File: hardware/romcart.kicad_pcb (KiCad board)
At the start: 4 copper layers, 57.5 x 51 mm, 29 parts, among them J1 GAME BOY 32 CONTACTS, M1 Core2350B2 (31692), Q1 2N7002, U1 SN74LVC245APWR, U2 SN74LVC245APWR, U3 SN74LVC245APWR, U4 SN74LVC8T245PWR, U5 SN74LVC1G10DBVR, U6 SN74LVC1G332DBVR

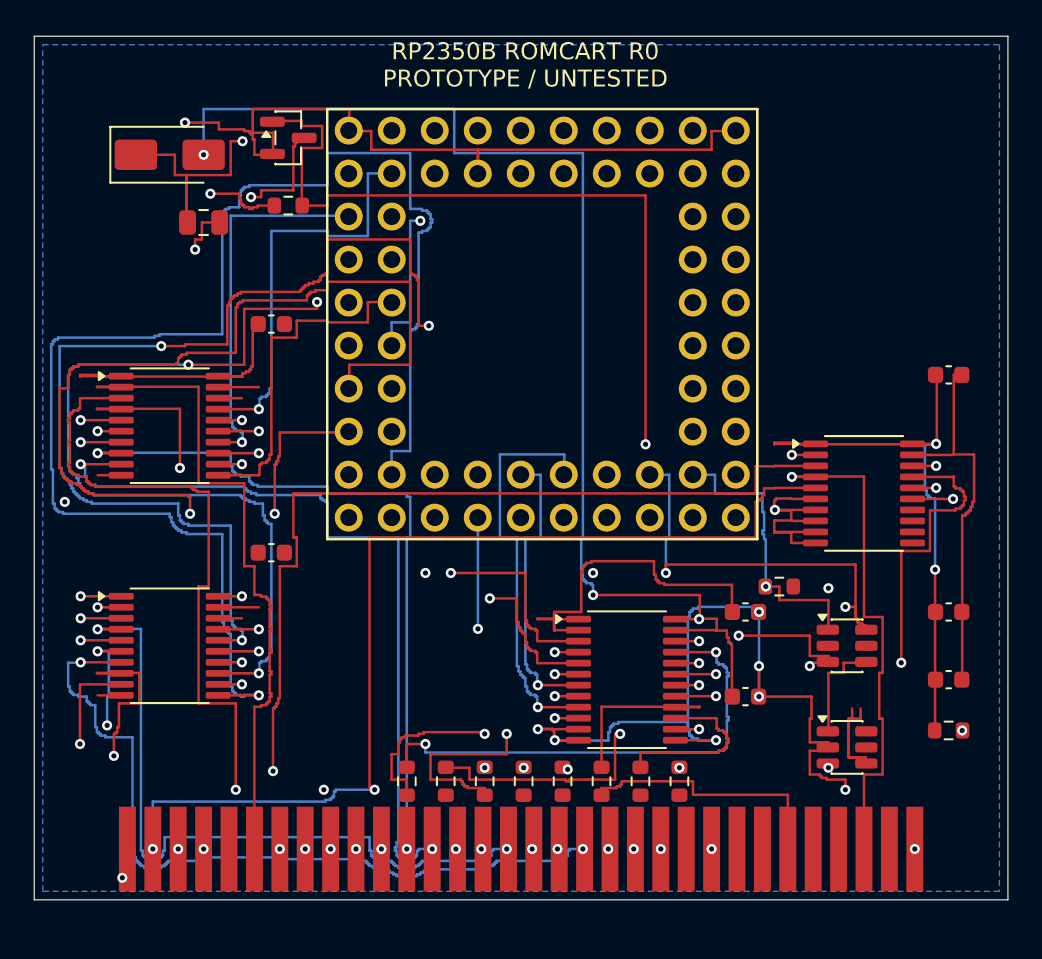
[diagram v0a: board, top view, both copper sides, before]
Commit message: Complete carrier routing and pass ERC DRC and schematic parity; refresh reviewed fabrication drafts
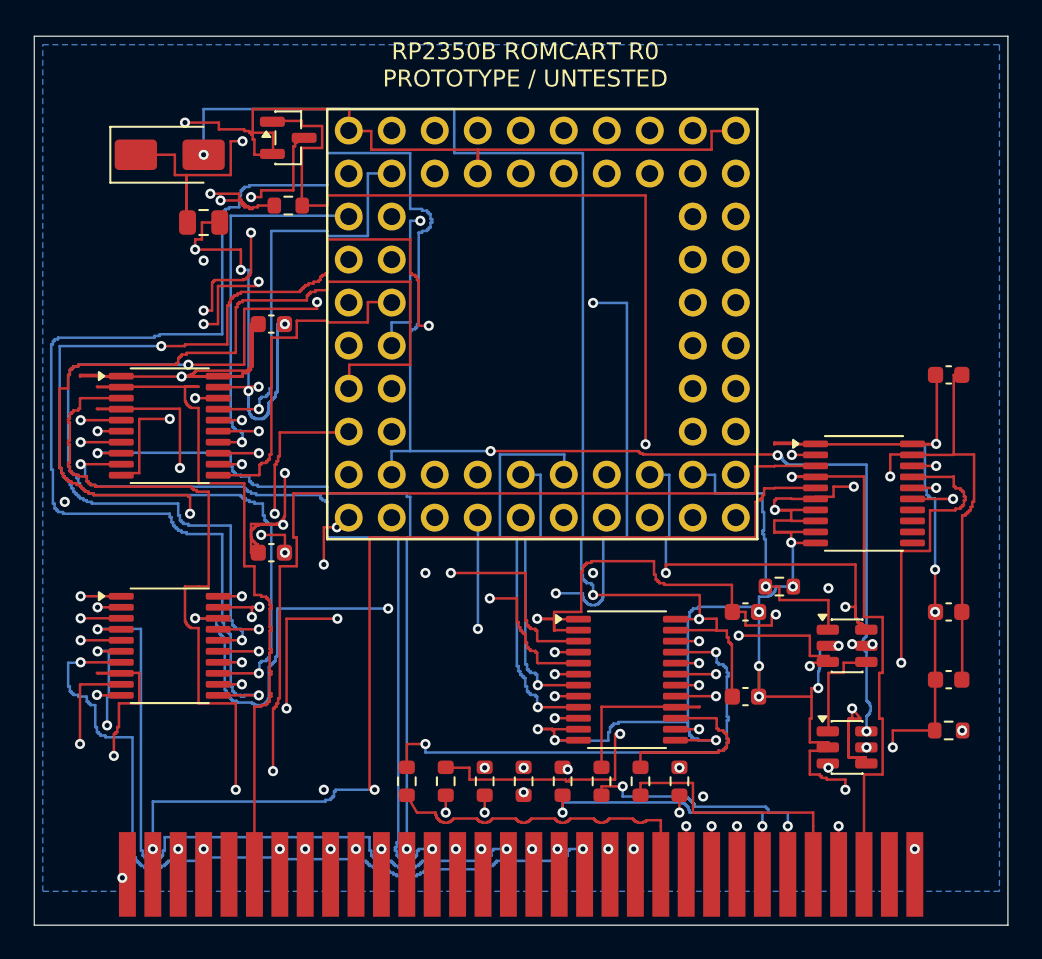
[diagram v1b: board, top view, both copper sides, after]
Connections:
- net +3V3 renamed /+3V3
- net +5V_GB renamed /+5V_GB
- net A0 renamed /A0
- net A0_3V3 renamed /A0_3V3
- net A1 renamed /A1
- net A10 renamed /A10
- net A10_3V3 renamed /A10_3V3
- net A11 renamed /A11
- net A11_3V3 renamed /A11_3V3
- net A12 renamed /A12
- net A12_3V3 renamed /A12_3V3
- net A13 renamed /A13
- net A13_3V3 renamed /A13_3V3
- net A14 renamed /A14
- net A14_3V3 renamed /A14_3V3
- net A15 renamed /A15
- net A15_3V3 renamed /A15_3V3
- net A1_3V3 renamed /A1_3V3
- net A2 renamed /A2
- net A2_3V3 renamed /A2_3V3
- net A3 renamed /A3
- net A3_3V3 renamed /A3_3V3
- net A4 renamed /A4
- net A4_3V3 renamed /A4_3V3
- net A5 renamed /A5
- net A5_3V3 renamed /A5_3V3
- net A6 renamed /A6
- net A6_3V3 renamed /A6_3V3
- net A7 renamed /A7
- net A7_3V3 renamed /A7_3V3
- net A8 renamed /A8
- net A8_3V3 renamed /A8_3V3
- net A9 renamed /A9
- net A9_3V3 renamed /A9_3V3
- net CLK renamed /CLK
- net CLK_3V3 renamed /CLK_3V3
- net D0 renamed /D0
- net D0_3V3 renamed /D0_3V3
- net D0_GB renamed /D0_GB
- net D1 renamed /D1
- net D1_3V3 renamed /D1_3V3
- net D1_GB renamed /D1_GB
- net D2 renamed /D2
- net D2_3V3 renamed /D2_3V3
- net D2_GB renamed /D2_GB
- net D3 renamed /D3
- net D3_3V3 renamed /D3_3V3
- net D3_GB renamed /D3_GB
- net D4 renamed /D4
- net D4_3V3 renamed /D4_3V3
- net D4_GB renamed /D4_GB
- net D5 renamed /D5
- net D5_3V3 renamed /D5_3V3
- net D5_GB renamed /D5_GB
- net D6 renamed /D6
- net D6_3V3 renamed /D6_3V3
- net D6_GB renamed /D6_GB
- net D7 renamed /D7
- net D7_3V3 renamed /D7_3V3
- net D7_GB renamed /D7_GB
- net GND renamed /GND
- net INHIBIT renamed /INHIBIT
- net MOD_VBUS renamed /MOD_VBUS
- net OE_L renamed /OE_L
- net RD_L renamed /RD_L
- net RD_L_3V3 renamed /RD_L_3V3
- net RESET_HOLD renamed /RESET_HOLD
- net RESET_L renamed /RESET_L
- net RESET_L_3V3 renamed /RESET_L_3V3
- net VALID renamed /VALID
- net WR_L renamed /WR_L
- net WR_L_3V3 renamed /WR_L_3V3
- J1 pad 31: (no net) -> unconnected-(J1-VIN-Pad31)
- J1 pad 5: (no net) -> unconnected-(J1-CS_L-Pad5)
- M1 pad 3V3_EN: (no net) -> unconnected-(M1-Pad3V3_EN)
- M1 pad ADC_VREF: (no net) -> unconnected-(M1-PadADC_VREF)
- M1 pad BOOTSEL: (no net) -> unconnected-(M1-PadBOOTSEL)
- M1 pad GP30: (no net) -> unconnected-(M1-PadGP30)
- M1 pad GP31: (no net) -> unconnected-(M1-PadGP31)
- M1 pad GP32: (no net) -> unconnected-(M1-PadGP32)
- M1 pad GP33: (no net) -> unconnected-(M1-PadGP33)
- M1 pad GP34: (no net) -> unconnected-(M1-PadGP34)
- M1 pad GP35: (no net) -> unconnected-(M1-PadGP35)
- M1 pad GP36: (no net) -> unconnected-(M1-PadGP36)
- M1 pad GP37: (no net) -> unconnected-(M1-PadGP37)
- M1 pad GP38: (no net) -> unconnected-(M1-PadGP38)
- M1 pad GP39: (no net) -> unconnected-(M1-PadGP39)
- M1 pad GP40: (no net) -> unconnected-(M1-PadGP40)
- M1 pad GP41: (no net) -> unconnected-(M1-PadGP41)
- M1 pad GP42: (no net) -> unconnected-(M1-PadGP42)
- M1 pad GP43: (no net) -> unconnected-(M1-PadGP43)
- M1 pad GP44: (no net) -> unconnected-(M1-PadGP44)
- M1 pad GP45: (no net) -> unconnected-(M1-PadGP45)
- M1 pad GP46: (no net) -> unconnected-(M1-PadGP46)
- M1 pad GP47: (no net) -> unconnected-(M1-PadGP47)
- M1 pad RUN: (no net) -> unconnected-(M1-PadRUN)
- M1 pad SWCLK: (no net) -> unconnected-(M1-PadSWCLK)
- M1 pad SWD: (no net) -> unconnected-(M1-PadSWD)
- M1 pad USB_DM: (no net) -> unconnected-(M1-PadUSB_DM)
- M1 pad USB_DP: (no net) -> unconnected-(M1-PadUSB_DP)
- U3 pad 11: (no net) -> unconnected-(U3-Pad11)
- U3 pad 12: (no net) -> unconnected-(U3-Pad12)
- U3 pad 13: (no net) -> unconnected-(U3-Pad13)
- U3 pad 14: (no net) -> unconnected-(U3-Pad14)
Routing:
- net /+3V3: track 131.4 -> 254.6 mm, vias 5 -> 20
- net /GND: track 198.6 -> 316.7 mm, vias 11 -> 31
- net /A8_3V3: track 1.40 -> 76.0 mm, vias 0 -> 4
- net /A15_3V3: track 90.9 -> 135.4 mm, vias 1 -> 4
- net /A0_3V3: track 1.40 -> 32.6 mm, vias 0 -> 2
- net /D1_GB: track 0.00 -> 21.7 mm, vias 0 -> 2
- net /D4_GB: track 0.00 -> 17.7 mm, vias 0 -> 2
- net /D3_GB: track 0.00 -> 17.6 mm, vias 0 -> 2
- net /D6_GB: track 0.00 -> 16.3 mm
- net /D7_GB: track 0.00 -> 16.0 mm, vias 0 -> 3
- net /D2_GB: track 30.2 -> 19.3 mm
- net /D0_GB: track 27.4 -> 22.0 mm, vias 2 -> 0
- net /A0: track 40.8 -> 42.4 mm
- net /A1: track 43.8 -> 45.4 mm
- net /D5_GB: track 15.8 -> 16.7 mm, vias 0 -> 2
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- added copper zone on B.Cu, net /GND
- added copper zone on In1.Cu, net /GND
- removed copper zone on B.Cu, net (none)
- removed copper zone on In1.Cu, net (none)
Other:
- board size 57.5 x 51 mm -> 57.5 x 52.5 mm
